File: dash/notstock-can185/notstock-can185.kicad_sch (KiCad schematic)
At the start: 31 parts, among them J1 OBD 12V GND H L, J2 to display UART, J3 5V to display, U1 LMR16006YDDCR, U2 TJA1051T/3

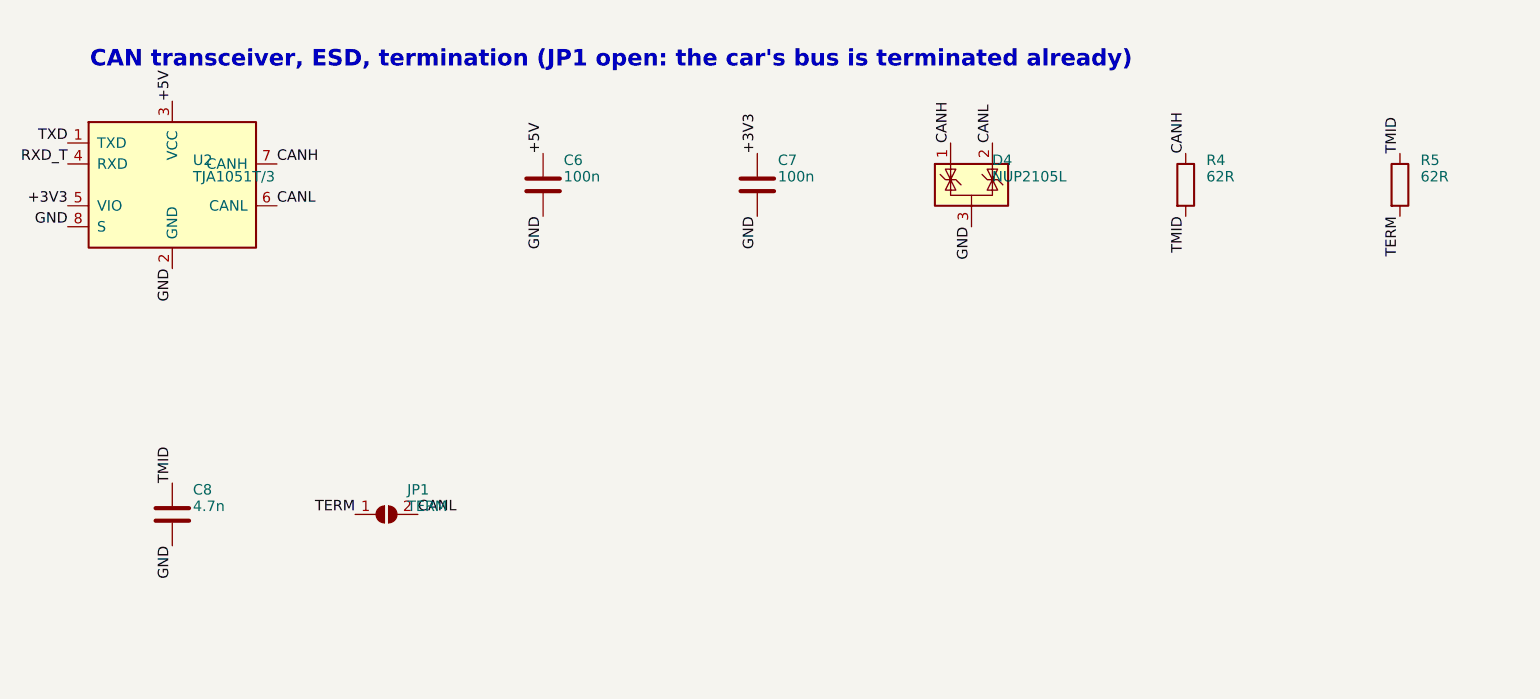
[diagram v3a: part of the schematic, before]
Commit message: CAN 1.85: termination R4/R5/C8 not assembled (no 60 R 0805 in stock)
Co-Authored-By: Claude Opus 5.5 <noreply@anthropic.com>
Claude-Session: https://claude.ai/code/session_018SKN4tJhAPpVCWtvRZgZpD
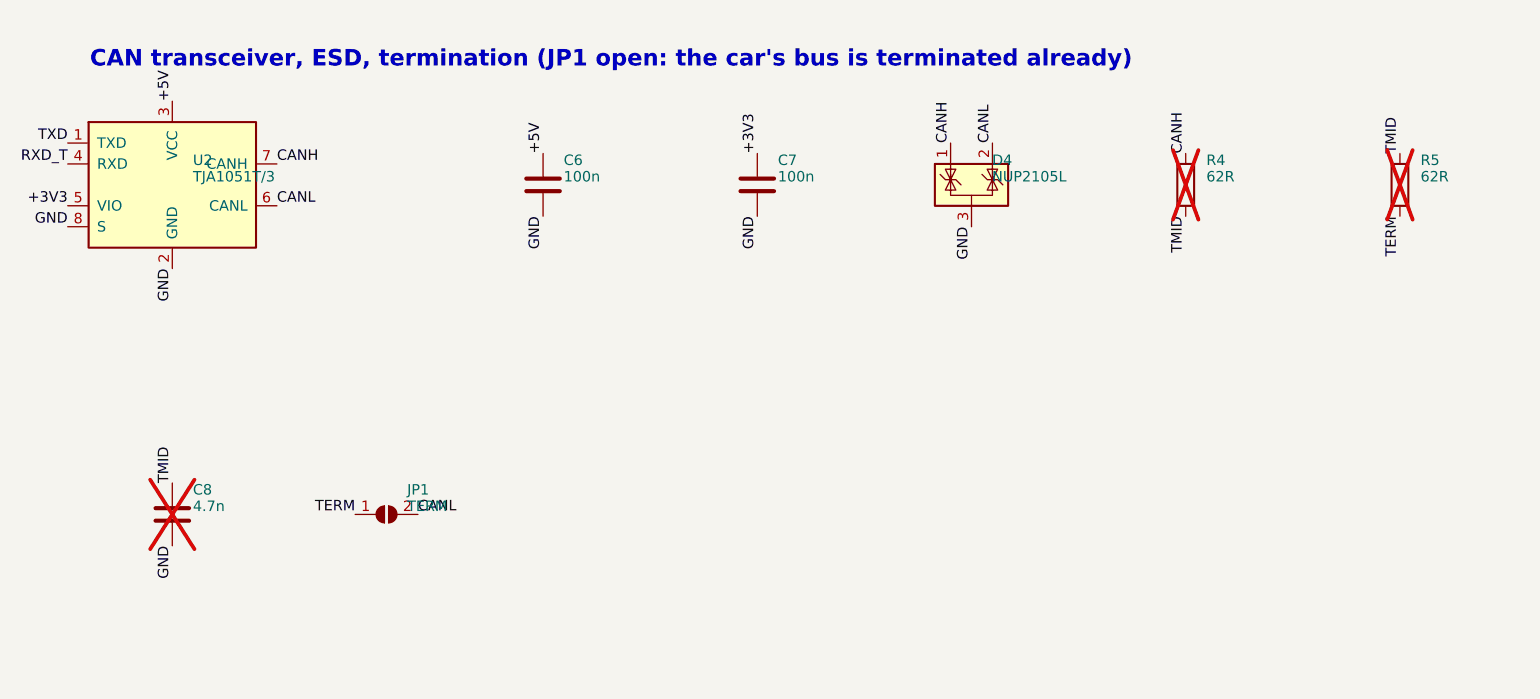
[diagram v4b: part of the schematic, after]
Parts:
- C8: now not fitted
- R4, R5: LCSC C5805111 -> (none); MPN Walsin MR08X62R0FTL (62 R 1%) -> 62 R 1% 0805; now not fitted
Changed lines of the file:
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@@
   )
   (symbol (lib_id "Device:R") (at 353 50 0) (unit 1)
-    (in_bom yes) (on_board yes) (dnp no)
+    (in_bom yes) (on_board yes) (dnp yes)
     (property "Reference" "R4" (at 355.5 47 0)
       (effects (font (size 1.27 1.27)) (justify left)))
@@
     (property "Datasheet" "~" (at 353 50 0)
       (effects (font (size 1.27 1.27)) hide))
-    (property "LCSC" "C5805111" (at 353 50 0)
-      (effects (font (size 1.27 1.27)) hide))
-    (property "MPN" "Walsin MR08X62R0FTL (62 R 1%)" (at 353 50 0)
+    (property "MPN" "62 R 1% 0805" (at 353 50 0)
       (effects (font (size 1.27 1.27)) hide))
     (pin "1")
@@
   )
   (symbol (lib_id "Device:R") (at 379 50 0) (unit 1)
-    (in_bom yes) (on_board yes) (dnp no)
+    (in_bom yes) (on_board yes) (dnp yes)
     (property "Reference" "R5" (at 381.5 47 0)
       (effects (font (size 1.27 1.27)) (justify left)))
@@
     (property "Datasheet" "~" (at 379 50 0)
       (effects (font (size 1.27 1.27)) hide))
-    (property "LCSC" "C5805111" (at 379 50 0)
-      (effects (font (size 1.27 1.27)) hide))
-    (property "MPN" "Walsin MR08X62R0FTL (62 R 1%)" (at 379 50 0)
+    (property "MPN" "62 R 1% 0805" (at 379 50 0)
       (effects (font (size 1.27 1.27)) hide))
     (pin "1")
@@
   )
   (symbol (lib_id "Device:C") (at 230 90 0) (unit 1)
-    (in_bom yes) (on_board yes) (dnp no)
+    (in_bom yes) (on_board yes) (dnp yes)
     (property "Reference" "C8" (at 232.5 87 0)
       (effects (font (size 1.27 1.27)) (justify left)))

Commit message: CAN 1.85 rev 4: power the display through its battery socket
12 V -> 3.75 V into the display's battery input on two wires instead of
5 V into its USB-C (no room for a cable). USB-C, CC resistors gone;
SN65HVD230 on the display's 3.3 V replaces the 5 V TJA1051T/3. The
display's Key1 must be bridged so its battery switch turns on.

Co-Authored-By: Claude Opus 5.5 <noreply@anthropic.com>
Claude-Session: https://claude.ai/code/session_018SKN4tJhAPpVCWtvRZgZpD
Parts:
- removed R7, R8: 56k, Resistor_SMD:R_0603_1608Metric, symbol Device:R
- J3: value 5V to display -> BAT to display; footprint Connector_USB:USB_C_Receptacle_HRO_TYPE-C-31-M-12 -> Connector_Wire:SolderWire-0.25sqmm_1x02_P4.2mm_D0.65mm_OD1.7mm; symbol Connector:USB_C_Receptacle_USB2.0_16P -> Connector_Generic:Conn_01x02; LCSC C165948 -> (none); MPN HRO TYPE-C-31-M-12 (USB-C, data pins open) -> (wires); now not fitted
- R2: value 56k -> 39k; LCSC C23206 -> C23153; MPN UNI-ROYAL 0603WAF5602T5E (56 k 1%) -> UNI-ROYAL 0603WAF3902T5E (39 k 1%)
- U2: value TJA1051T/3 -> SN65HVD230; symbol Interface_CAN_LIN:TJA1051T-3 -> Interface_CAN_LIN:SN65HVD230; LCSC C38695 -> C12084; MPN NXP TJA1051T/3/1J -> TI SN65HVD230DR
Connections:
- net +3V3: now also C6.1, U2.3 (VCC); no longer U2.5 (VIO)
- net GND: now also J3.2 (Pin_2); no longer J3.A1 (GND), J3.A12 (GND), J3.B1 (GND), J3.B12 (GND), J3.S1 (SHIELD)
- removed net +5V: C4.1, C5.1, C6.1, J3.A4 (VBUS), J3.A9 (VBUS), J3.B4 (VBUS), J3.B9 (VBUS), L1.2, R2.1, U2.3 (VCC)
- removed net CC1: J3.A5 (CC1)
- removed net CC2: J3.B5 (CC2)
- new net BAT_LCD: C4.1, C5.1, J3.1 (Pin_1), L1.2, R2.1
- no-connect marks 6 -> 1
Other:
- note added: "12 V -> 3.75 V for the display's battery input"
- note added: "To the display ESP32-S3-Touch-LCD-1.85: UART socket (SH 1.0 cable, 1:1) and battery socket (wires, MX1.25 plug; bridge the display's Key1)"
- note removed: "12 V -> 5 V"
- note removed: "To the display ESP32-S3-Touch-LCD-1.85: UART socket (SH 1.0 cable, 1:1) and USB-C (5 V)"
- moved on the sheet: U2

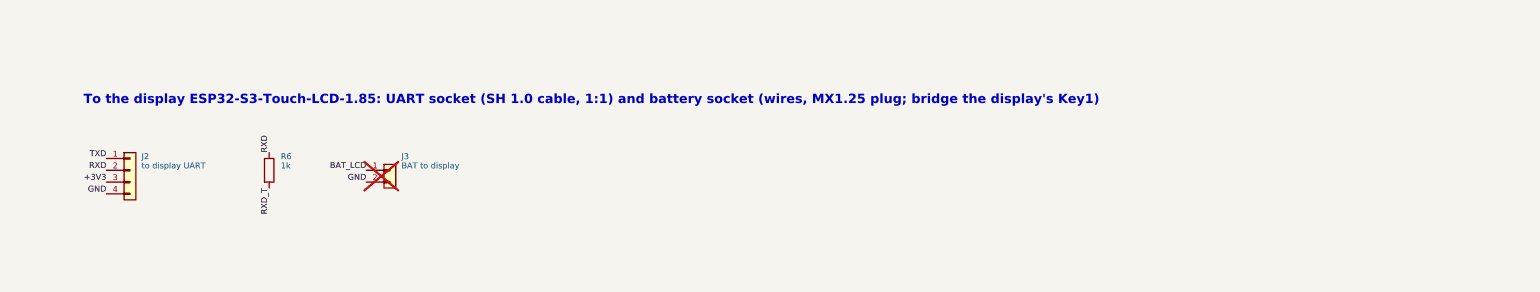
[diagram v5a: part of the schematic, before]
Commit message: CAN 1.85 rev 4: UART cable soldered to pads instead of an SH socket
The display comes with a cable plugged into its UART socket; its free
ends are soldered to J2 now, marked with the display's names. J3 labels
moved onto its pads. R6 moved for the labels.

Co-Authored-By: Claude Opus 5.5 <noreply@anthropic.com>
Claude-Session: https://claude.ai/code/session_018SKN4tJhAPpVCWtvRZgZpD
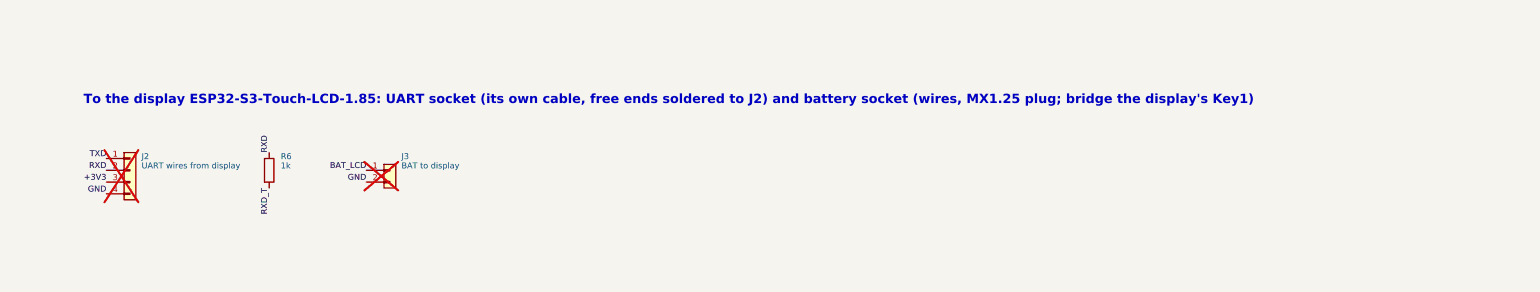
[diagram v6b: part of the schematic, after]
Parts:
- J2: value to display UART -> UART wires from display; footprint Connector_JST:JST_SH_BM04B-SRSS-TB_1x04-1MP_P1.00mm_Vertical -> Connector_Wire:SolderWire-0.15sqmm_1x04_P4mm_D0.5mm_OD1.5mm; LCSC C160390 -> (none); MPN JST BM04B-SRSS-TB(LF)(SN) -> (wires); now not fitted
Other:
- note added: "To the display ESP32-S3-Touch-LCD-1.85: UART socket (its own cable, free ends soldered to J2) and battery socket (wires, MX1.25 plug; bridge the display's Key1)"
- note removed: "To the display ESP32-S3-Touch-LCD-1.85: UART socket (SH 1.0 cable, 1:1) and battery socket (wires, MX1.25 plug; bridge the display's Key1)"
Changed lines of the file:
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@@
     (effects (font (size 1.27 1.27)) (justify left bottom))
   )
-  (text "To the display ESP32-S3-Touch-LCD-1.85: UART socket (SH 1.0 cable, 1:1) and battery socket (wires, MX1.25 plug; bridge the display's Key1)" (at 220 158 0)
+  (text "To the display ESP32-S3-Touch-LCD-1.85: UART socket (its own cable, free ends soldered to J2) and battery socket (wires, MX1.25 plug; bridge the display's Key1)" (at 220 158 0)
     (effects (font (size 2 2) bold) (justify left bottom))
   )
   (symbol (lib_id "Connector_Generic:Conn_01x04") (at 230 172 0) (unit 1)
-    (in_bom yes) (on_board yes) (dnp no)
+    (in_bom yes) (on_board yes) (dnp yes)
     (property "Reference" "J2" (at 232.5 169 0)
       (effects (font (size 1.27 1.27)) (justify left)))
-    (property "Value" "to display UART" (at 232.5 171 0)
+    (property "Value" "UART wires from display" (at 232.5 171 0)
       (effects (font (size 1.27 1.27)) (justify left)))
-    (property "Footprint" "Connector_JST:JST_SH_BM04B-SRSS-TB_1x04-1MP_P1.00mm_Vertical" (at 230 172 0)
+    (property "Footprint" "Connector_Wire:SolderWire-0.15sqmm_1x04_P4mm_D0.5mm_OD1.5mm" (at 230 172 0)
       (effects (font (size 1.27 1.27)) hide))
     (property "Datasheet" "~" (at 230 172 0)
       (effects (font (size 1.27 1.27)) hide))
-    (property "LCSC" "C160390" (at 230 172 0)
-      (effects (font (size 1.27 1.27)) hide))
-    (property "MPN" "JST BM04B-SRSS-TB(LF)(SN)" (at 230 172 0)
+    (property "MPN" "(wires)" (at 230 172 0)
       (effects (font (size 1.27 1.27)) hide))
     (pin "1")

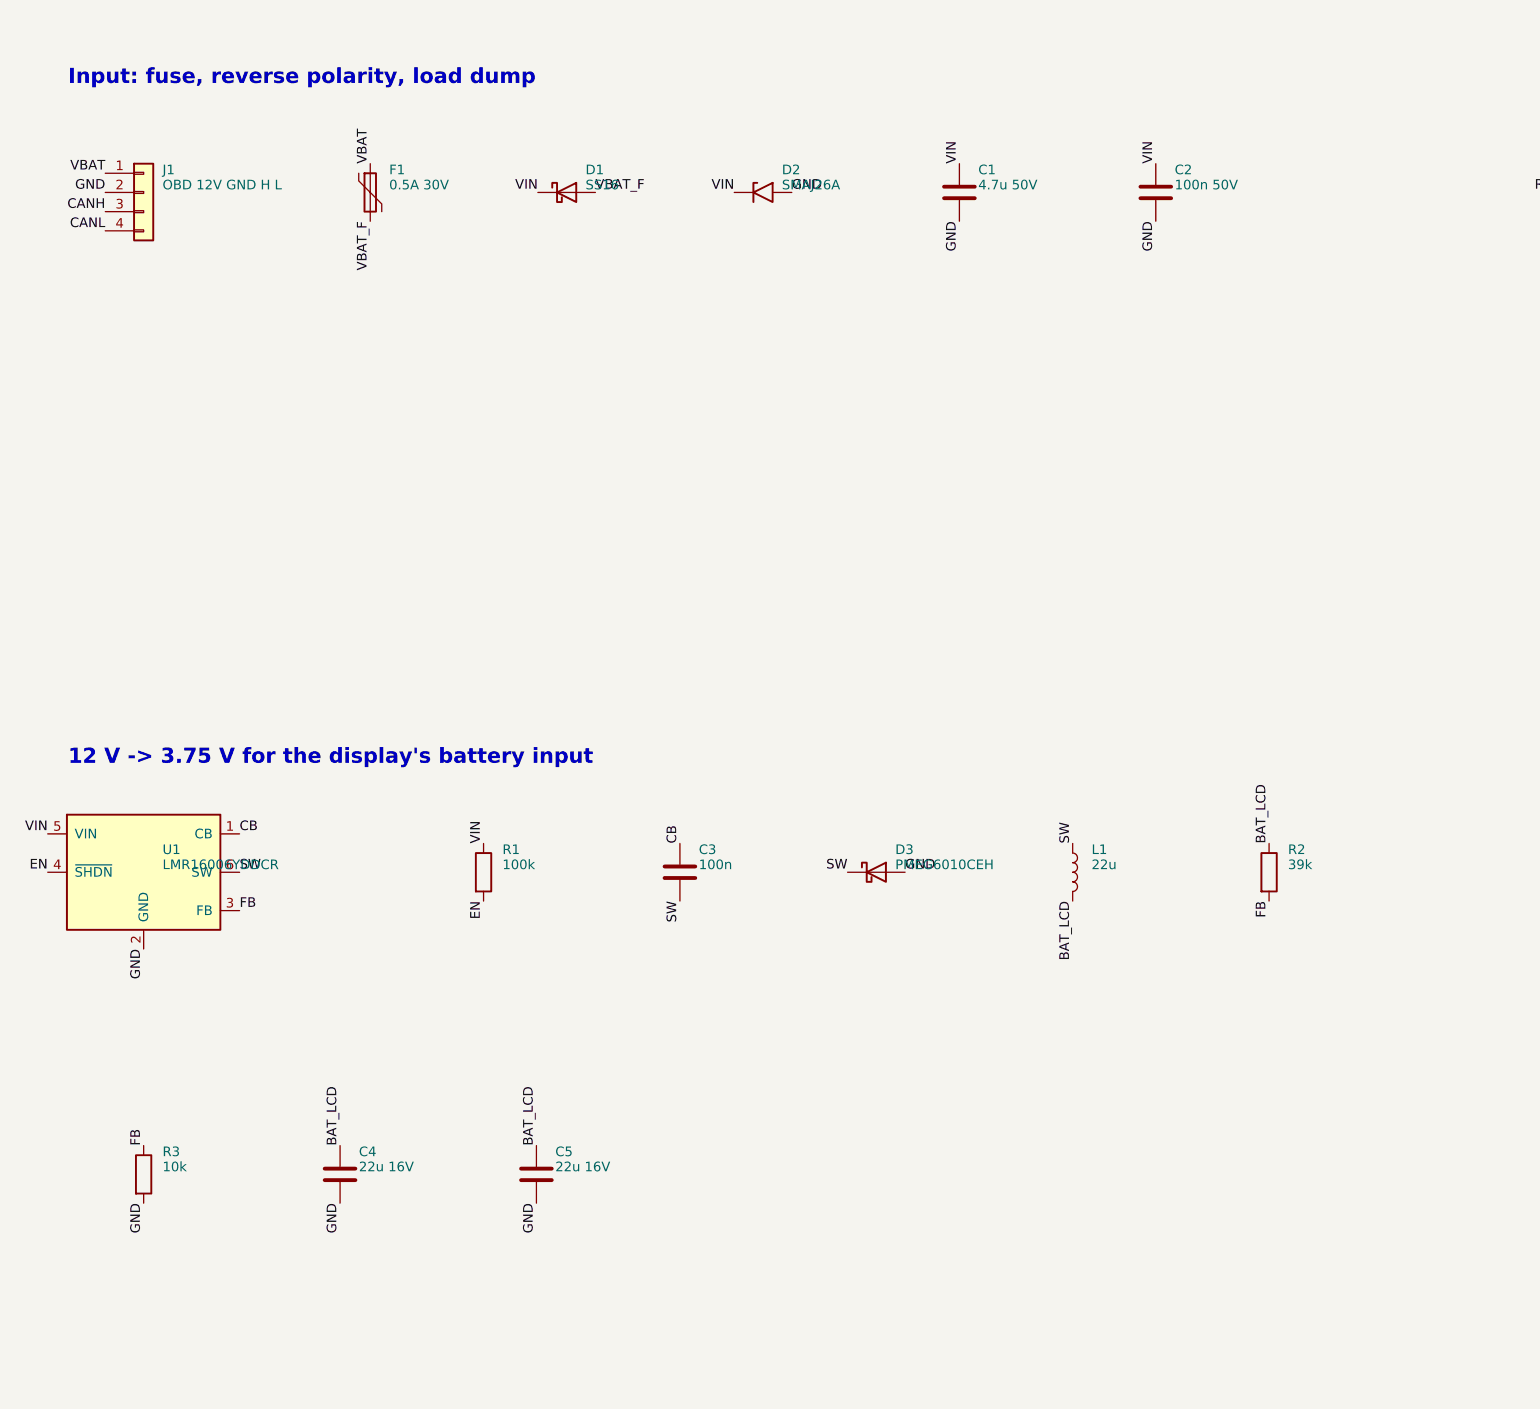
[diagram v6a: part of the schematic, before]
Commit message: CAN 1.85 rev 5: on and off with the key through the K-line
OBD pin 7 onto the regulator's EN through 100 k / 13 k (on above 10.5 V,
off below 9.3 V), 100 nF against K-line traffic. J1 becomes a 5-pin JST PH,
vertical.

Co-Authored-By: Claude Opus 5.5 <noreply@anthropic.com>
Claude-Session: https://claude.ai/code/session_018SKN4tJhAPpVCWtvRZgZpD
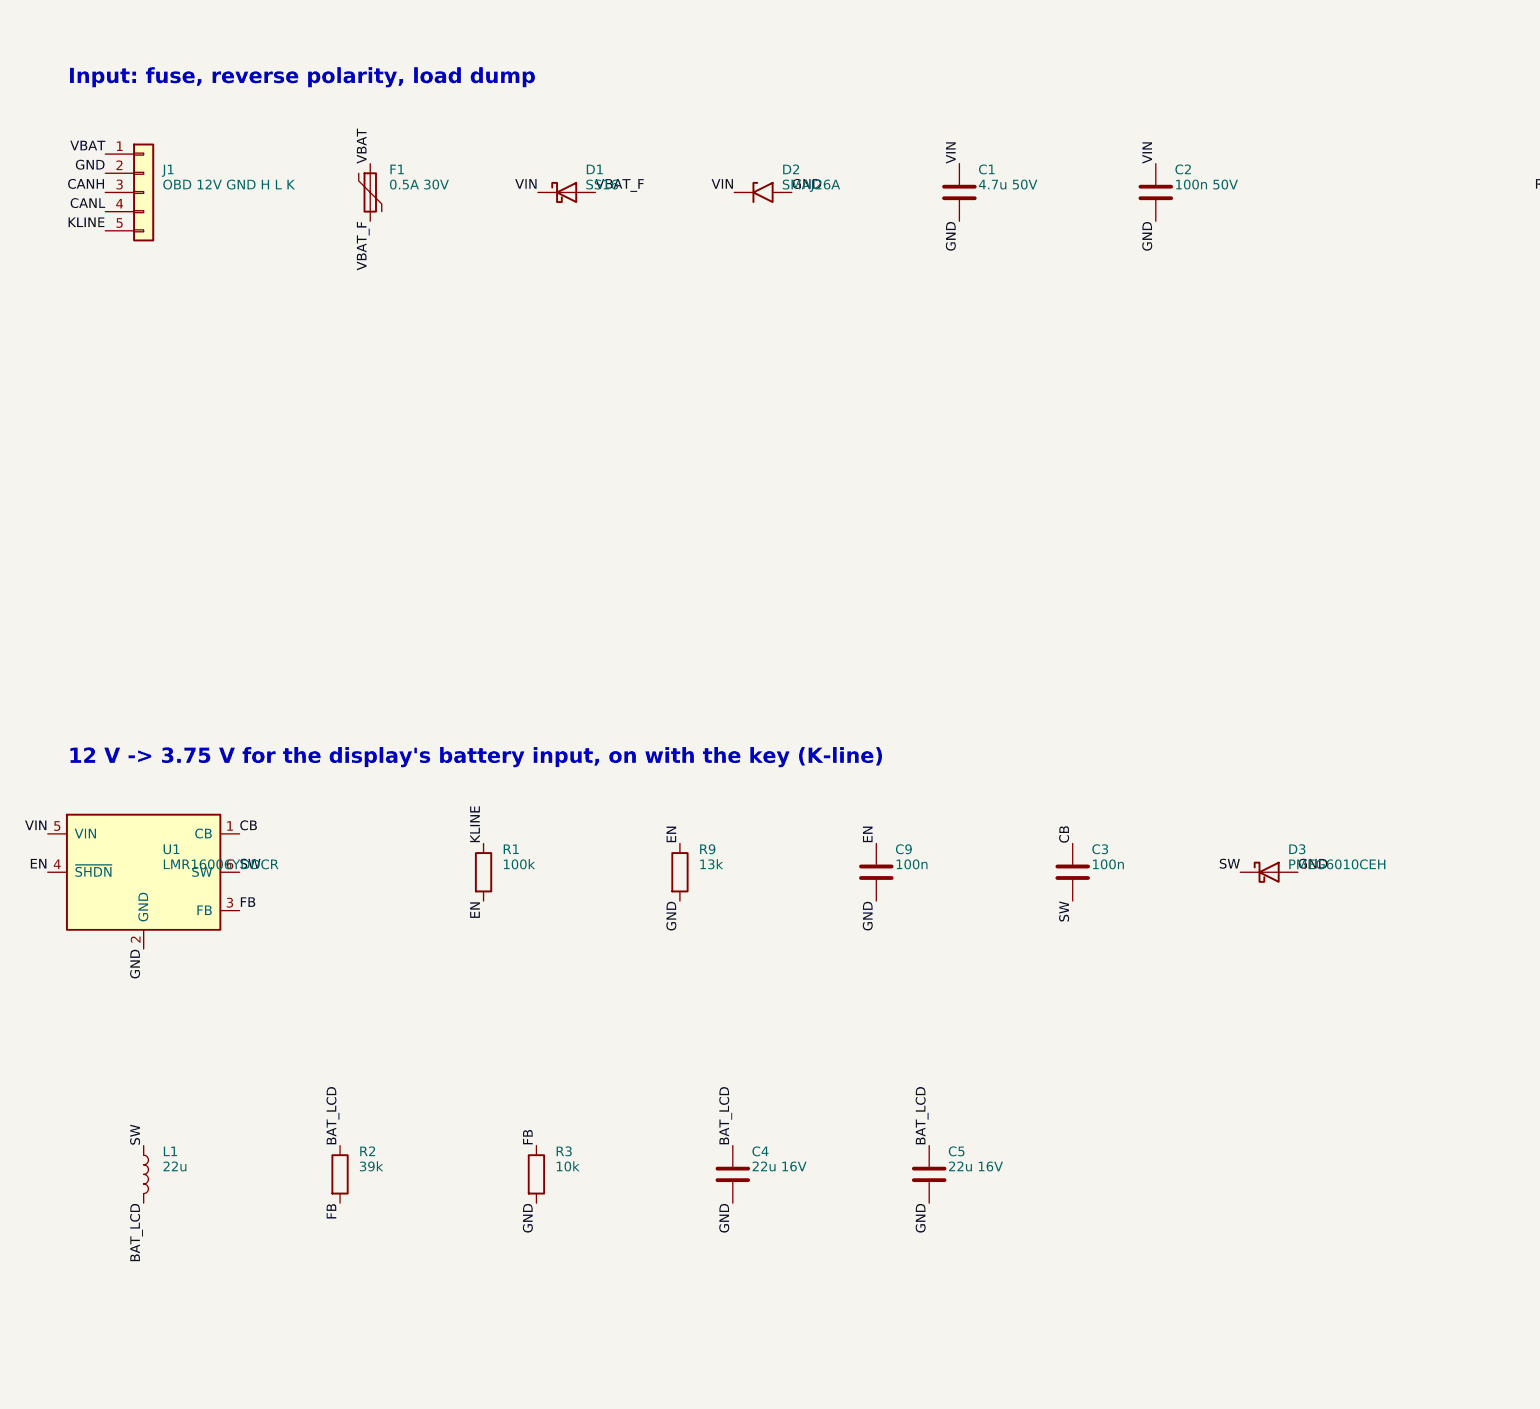
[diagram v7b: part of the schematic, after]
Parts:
- added C9: 100n, Capacitor_SMD:C_0603_1608Metric, symbol Device:C
- added R9: 13k, Resistor_SMD:R_0603_1608Metric, symbol Device:R
- J1: value OBD 12V GND H L -> OBD 12V GND H L K; footprint Connector_JST:JST_PH_B4B-PH-SM4-TB_1x04-1MP_P2.00mm_Vertical -> Connector_JST:JST_PH_B5B-PH-SM4-TB_1x05-1MP_P2.00mm_Vertical; symbol Connector_Generic:Conn_01x04 -> Connector_Generic:Conn_01x05; LCSC C160354 -> C265085; MPN JST B4B-PH-SM4-TB(LF)(SN) -> JST B5B-PH-SM4-TB(LF)(SN)
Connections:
- net EN: now also C9.1, R9.1
- net GND: now also C9.2, R9.2
- net VIN: no longer R1.1
- new net KLINE: J1.5 (Pin_5), R1.1
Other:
- note added: "12 V -> 3.75 V for the display's battery input, on with the key (K-line)"
- note removed: "12 V -> 3.75 V for the display's battery input"
- moved on the sheet: C3, C4, C5, D3, L1, R2, R3
